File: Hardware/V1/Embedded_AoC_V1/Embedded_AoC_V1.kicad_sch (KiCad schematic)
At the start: 94 parts, among them IC1 STM32H533ZET6, IC4 ADP2302ARDZ-3.3-R7, IC8 AS6C6416-55TIN, J1 PRT-10811, J2 UJ2-BH-W1-TH, J3 TST-110-01-F-D, J4 MSD-1-A, J5 67996-100HLF, Q1001 NSS30101LT1G, Q801 RUM001L02T2CL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

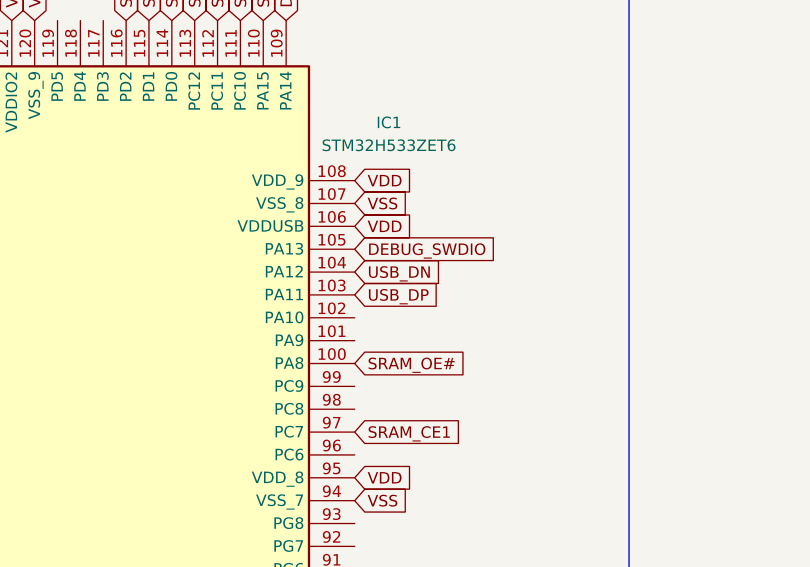
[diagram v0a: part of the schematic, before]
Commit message: Added STM32 project and fixed pinning (USB DP/DN swapped)
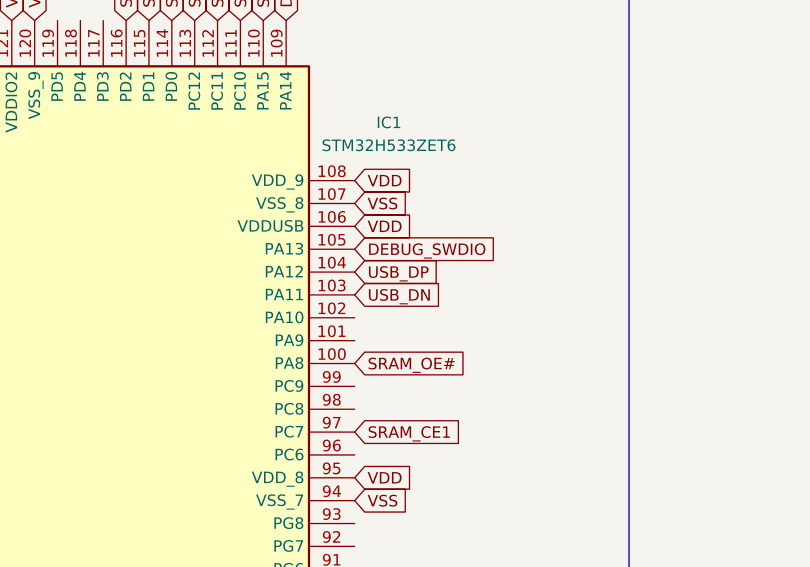
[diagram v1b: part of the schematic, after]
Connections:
- net USB_DN: now also IC1.103 (PA11); no longer IC1.104 (PA12)
- net USB_DP: now also IC1.104 (PA12); no longer IC1.103 (PA11)

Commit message: Released hardware
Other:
- note removed: "ADD ESD PROTECTION ON USER BUTTONS"
- moved on the sheet: C1, C10, C11, C12, C13, C14, C15, C17, C18, C19, C20, C21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
